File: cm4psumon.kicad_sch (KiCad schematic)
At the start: 4 parts, among them U6 INA260

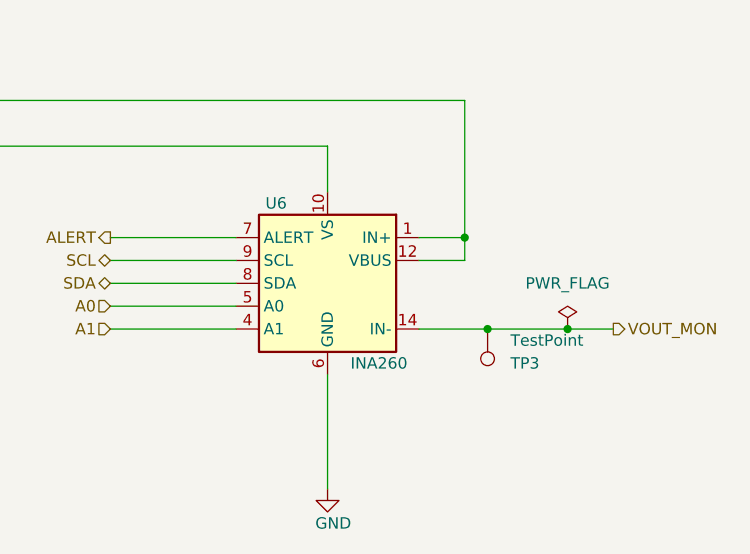
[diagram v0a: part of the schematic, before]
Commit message: added ti buffer lib
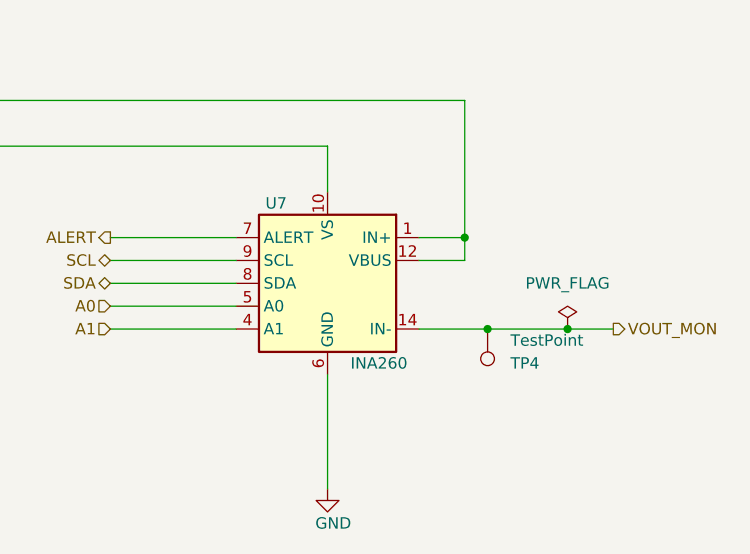
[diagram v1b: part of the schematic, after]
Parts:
- renumbered TP3 to TP4, U6 to U7
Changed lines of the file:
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@@
   (symbol (lib_id "Sensor_I2C_TI:INA260") (at 125.73 67.31 0) (mirror y)
     (in_bom yes) (on_board yes)
-    (property "Reference" "U6" (id 0) (at 120.015 58.42 0))
+    (property "Reference" "U7" (id 0) (at 120.015 58.42 0))
     (property "Value" "INA260" (id 1) (at 131.445 76.2 0))
     (property "Footprint" "Sensor_I2C_TI:TSSOP-16_4.4x5mm_P0.65mm_pin1" (id 2) (at 124.46 99.06 0)
@@
   (symbol (lib_id "power:GND") (at 125.73 90.17 0)
     (in_bom yes) (on_board yes)
-    (property "Reference" "#PWR020" (id 0) (at 125.73 96.52 0)
+    (property "Reference" "#PWR022" (id 0) (at 125.73 96.52 0)
       (effects (font (size 1.27 1.27)) hide)
     )
@@
   (symbol (lib_id "power:GND") (at 69.85 68.58 0)
     (in_bom yes) (on_board yes) (fields_autoplaced)
-    (property "Reference" "#PWR019" (id 0) (at 69.85 74.93 0)
+    (property "Reference" "#PWR021" (id 0) (at 69.85 74.93 0)
       (effects (font (size 1.27 1.27)) hide)
     )
@@
   (symbol (lib_id "Connector:TestPoint") (at 143.51 72.39 0) (mirror x)
     (in_bom yes) (on_board yes)
-    (property "Reference" "TP3" (id 0) (at 146.05 76.2 0)
+    (property "Reference" "TP4" (id 0) (at 146.05 76.2 0)
       (effects (font (size 1.27 1.27)) (justify left))
     )

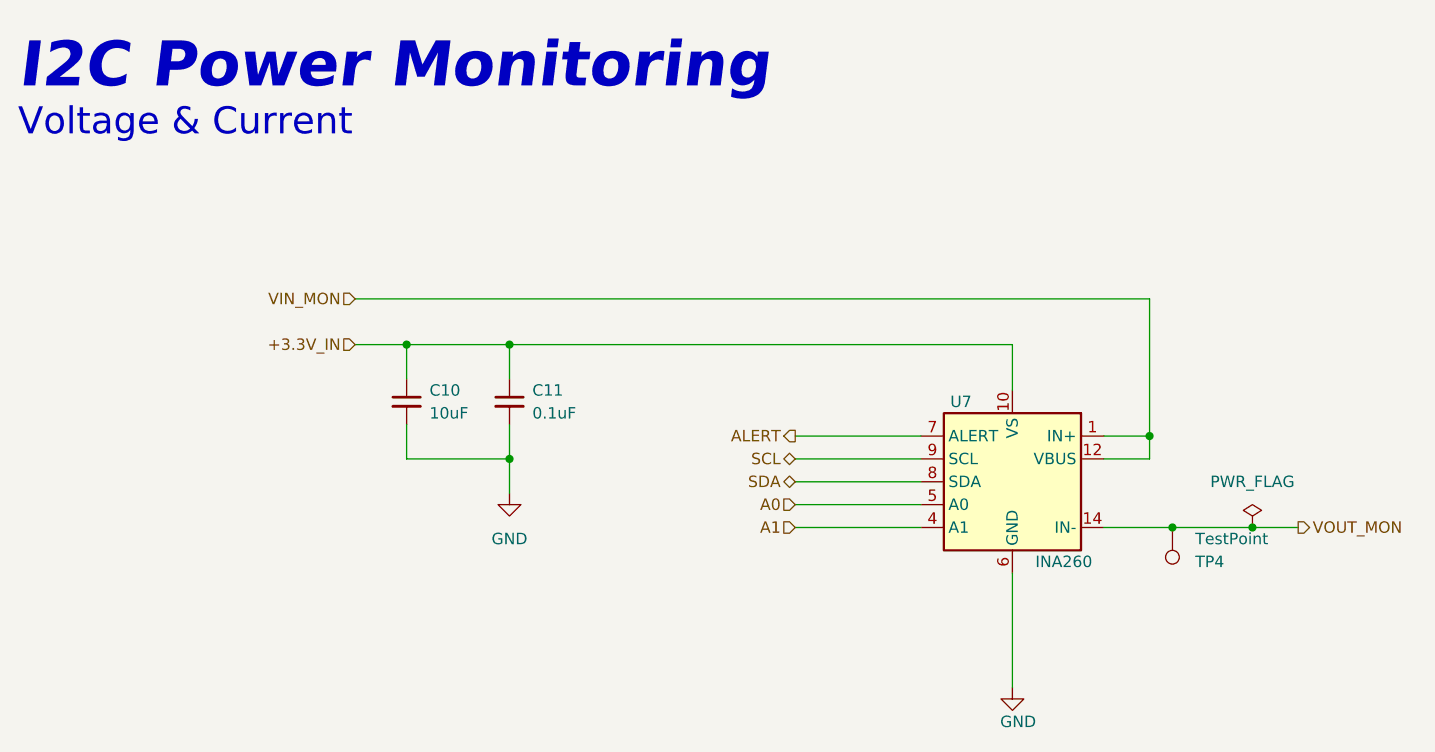
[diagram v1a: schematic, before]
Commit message: initial integration of i2c arbiter
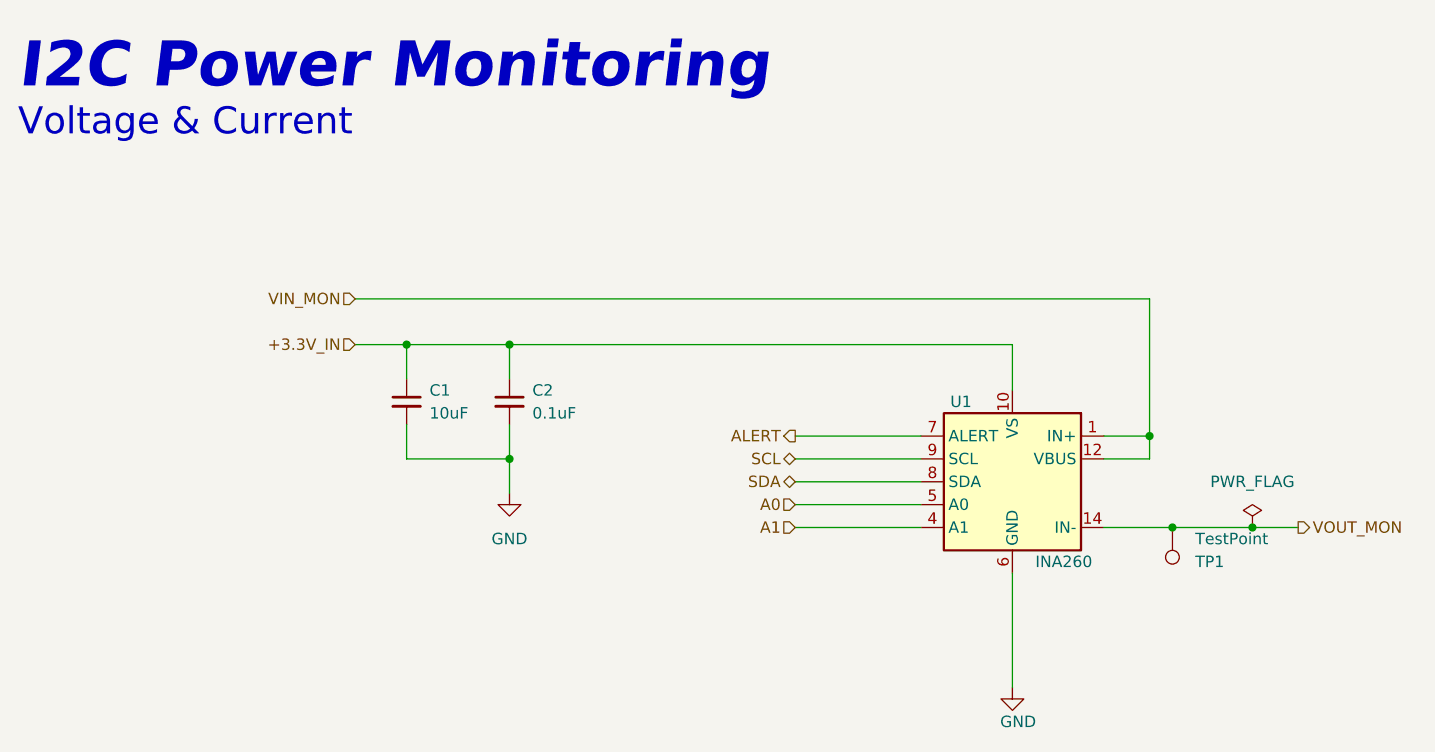
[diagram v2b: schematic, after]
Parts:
- renumbered C10 to C1, C11 to C2, TP4 to TP1, U7 to U1
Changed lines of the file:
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@@
   (symbol (lib_id "Sensor_I2C_TI:INA260") (at 125.73 67.31 0) (mirror y)
     (in_bom yes) (on_board yes)
-    (property "Reference" "U7" (id 0) (at 120.015 58.42 0))
+    (property "Reference" "U1" (id 0) (at 120.015 58.42 0))
     (property "Value" "INA260" (id 1) (at 131.445 76.2 0))
     (property "Footprint" "Sensor_I2C_TI:TSSOP-16_4.4x5mm_P0.65mm_pin1" (id 2) (at 124.46 99.06 0)
@@
   (symbol (lib_id "power:GND") (at 125.73 90.17 0)
     (in_bom yes) (on_board yes)
-    (property "Reference" "#PWR022" (id 0) (at 125.73 96.52 0)
+    (property "Reference" "#PWR03" (id 0) (at 125.73 96.52 0)
       (effects (font (size 1.27 1.27)) hide)
     )
@@
   (symbol (lib_id "power:PWR_FLAG") (at 152.4 72.39 0)
     (in_bom yes) (on_board yes) (fields_autoplaced)
-    (property "Reference" "#FLG04" (id 0) (at 152.4 70.485 0)
+    (property "Reference" "#FLG03" (id 0) (at 152.4 70.485 0)
       (effects (font (size 1.27 1.27)) hide)
     )
@@
   (symbol (lib_id "power:GND") (at 69.85 68.58 0)
     (in_bom yes) (on_board yes) (fields_autoplaced)
-    (property "Reference" "#PWR021" (id 0) (at 69.85 74.93 0)
+    (property "Reference" "#PWR02" (id 0) (at 69.85 74.93 0)
       (effects (font (size 1.27 1.27)) hide)
     )
@@
   (symbol (lib_id "Device:C_Small") (at 69.85 58.42 0)
     (in_bom yes) (on_board yes) (fields_autoplaced)
-    (property "Reference" "C11" (id 0) (at 72.39 57.1562 0)
+    (property "Reference" "C2" (id 0) (at 72.39 57.1562 0)
       (effects (font (size 1.27 1.27)) (justify left))
     )
@@
   (symbol (lib_id "Device:C_Small") (at 58.42 58.42 0)
     (in_bom yes) (on_board yes) (fields_autoplaced)
-    (property "Reference" "C10" (id 0) (at 60.96 57.1562 0)
+    (property "Reference" "C1" (id 0) (at 60.96 57.1562 0)
       (effects (font (size 1.27 1.27)) (justify left))
     )
@@
   (symbol (lib_id "Connector:TestPoint") (at 143.51 72.39 0) (mirror x)
     (in_bom yes) (on_board yes)
-    (property "Reference" "TP4" (id 0) (at 146.05 76.2 0)
+    (property "Reference" "TP1" (id 0) (at 146.05 76.2 0)
       (effects (font (size 1.27 1.27)) (justify left))
     )

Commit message: fixed I2C ping indicator
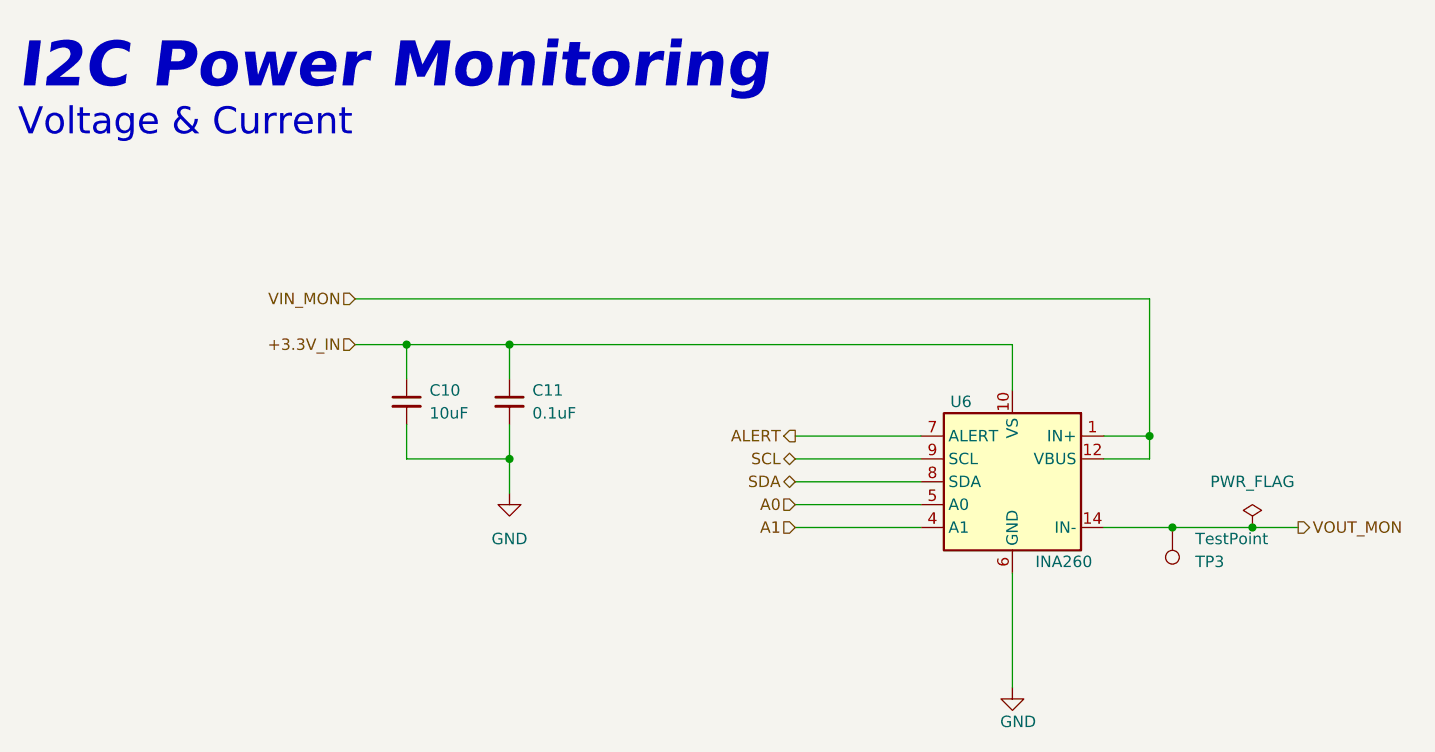
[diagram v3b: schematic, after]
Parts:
- renumbered C1 to C10, C2 to C11, TP1 to TP3, U1 to U6
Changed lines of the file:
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@@
   (symbol (lib_id "Sensor_I2C_TI:INA260") (at 125.73 67.31 0) (mirror y)
     (in_bom yes) (on_board yes)
-    (property "Reference" "U1" (id 0) (at 120.015 58.42 0))
+    (property "Reference" "U6" (id 0) (at 120.015 58.42 0))
     (property "Value" "INA260" (id 1) (at 131.445 76.2 0))
     (property "Footprint" "Sensor_I2C_TI:TSSOP-16_4.4x5mm_P0.65mm_pin1" (id 2) (at 124.46 99.06 0)
@@
   (symbol (lib_id "power:GND") (at 125.73 90.17 0)
     (in_bom yes) (on_board yes)
-    (property "Reference" "#PWR03" (id 0) (at 125.73 96.52 0)
+    (property "Reference" "#PWR020" (id 0) (at 125.73 96.52 0)
       (effects (font (size 1.27 1.27)) hide)
     )
@@
   (symbol (lib_id "power:PWR_FLAG") (at 152.4 72.39 0)
     (in_bom yes) (on_board yes) (fields_autoplaced)
-    (property "Reference" "#FLG03" (id 0) (at 152.4 70.485 0)
+    (property "Reference" "#FLG04" (id 0) (at 152.4 70.485 0)
       (effects (font (size 1.27 1.27)) hide)
     )
@@
   (symbol (lib_id "power:GND") (at 69.85 68.58 0)
     (in_bom yes) (on_board yes) (fields_autoplaced)
-    (property "Reference" "#PWR02" (id 0) (at 69.85 74.93 0)
+    (property "Reference" "#PWR019" (id 0) (at 69.85 74.93 0)
       (effects (font (size 1.27 1.27)) hide)
     )
@@
   (symbol (lib_id "Device:C_Small") (at 69.85 58.42 0)
     (in_bom yes) (on_board yes) (fields_autoplaced)
-    (property "Reference" "C2" (id 0) (at 72.39 57.1562 0)
+    (property "Reference" "C11" (id 0) (at 72.39 57.1562 0)
       (effects (font (size 1.27 1.27)) (justify left))
     )
@@
   (symbol (lib_id "Device:C_Small") (at 58.42 58.42 0)
     (in_bom yes) (on_board yes) (fields_autoplaced)
-    (property "Reference" "C1" (id 0) (at 60.96 57.1562 0)
+    (property "Reference" "C10" (id 0) (at 60.96 57.1562 0)
       (effects (font (size 1.27 1.27)) (justify left))
     )
@@
   (symbol (lib_id "Connector:TestPoint") (at 143.51 72.39 0) (mirror x)
     (in_bom yes) (on_board yes)
-    (property "Reference" "TP1" (id 0) (at 146.05 76.2 0)
+    (property "Reference" "TP3" (id 0) (at 146.05 76.2 0)
       (effects (font (size 1.27 1.27)) (justify left))
     )
